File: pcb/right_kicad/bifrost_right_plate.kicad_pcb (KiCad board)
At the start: 2 copper layers, 148.8 x 87.6 mm, 23 parts

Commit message: Update PCB designs
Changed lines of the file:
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@@
 			(layer "F.SilkS"
 				(type "Top Silk Screen")
+				(color "White")
 			)
 			(layer "F.Paste"
@@
 			(layer "F.Mask"
 				(type "Top Solder Mask")
+				(color "Black")
 				(thickness 0.01)
 			)
@@
 			(layer "dielectric 1"
 				(type "core")
+				(color "Aluminum")
 				(thickness 1.11)
 				(material "FR4")
@@
 			(layer "B.Mask"
 				(type "Bottom Solder Mask")
+				(color "Black")
 				(thickness 0.01)
 			)
@@
 			(layer "B.SilkS"
 				(type "Bottom Silk Screen")
+				(color "White")
 			)
 			(copper_finish "None")
@@
 		(capping no)
 		(filling no)
+		(zone_defaults)
 		(pcbplotparams
 			(layerselection 0x00000000_00000000_55555555_5755f5ff)
@@
 		(end -134.542277 8.653086)
 		(stroke
-			(width 0)
+			(width 0.1)
 			(type default)
 		)
@@
 		(end -136.326562 11.380429)
 		(stroke
-			(width 0)
+			(width 0.1)
 			(type default)
 		)
@@
 		(end -136.326563 72.209898)
 		(stroke
-			(width 0)
+			(width 0.1)
 			(type default)
 		)
@@
 		(end -135.961405 73.638355)
 		(stroke
-			(width 0)
+			(width 0.1)
 			(type default)
 		)
@@
 		(end -33.3375 -12.501562)
 		(stroke
-			(width 0)
+			(width 0.1)
 			(type default)
 		)
@@
 		(end -135.56636 74.360548)
 		(stroke
-			(width 0)
+			(width 0.1)
 			(type default)
 		)
@@
 		(end -133.349999 70.238699)
 		(stroke
-			(width 0)
+			(width 0.1)
 			(type default)
 		)
@@
 		(end -133.681091 74.91259)
 		(stroke
-			(width 0)
+			(width 0.1)
 			(type default)
 		)
@@
 		(end -53.80468 48.117266)
 		(stroke
-			(width 0)
+			(width 0.1)
 			(type default)
 		)
@@
 		(end -116.679234 3.694859)
 		(stroke
-			(width 0)
+			(width 0.1)
 			(type default)
 		)
@@
 		(end -50.119883 50.915685)
 		(stroke
-			(width 0)
+			(width 0.1)
 			(type default)
 		)
@@
 		(end -50.119883 50.915685)
 		(stroke
-			(width 0)
+			(width 0.1)
 			(type default)
 		)
@@
 		(end -47.10797 68.939307)
 		(stroke
-			(width 0)
+			(width 0.1)
 			(type default)
 		)
@@
 		(end 9.525 -12.501563)
 		(stroke
-			(width 0)
+			(width 0.1)
 			(type default)
 		)
@@
 		(end -45.637701 70.0958)
 		(stroke
-			(width 0)
+			(width 0.1)
 			(type default)
 		)
@@
 		(end 12.501563 -9.525)
 		(stroke
-			(width 0)
+			(width 0.1)
 			(type default)
 		)
@@
 		(end 9.525 -10.625)
 		(stroke
-			(width 0)
+			(width 0.1)
 			(type default)
 		)
@@
 		(end 9.525 65.575)
 		(stroke
-			(width 0)
+			(width 0.1)
 			(type default)
 		)
@@
 		(end -33.3375 69.651563)
 		(stroke
-			(width 0)
+			(width 0.1)
 			(type default)
 		)
@@
 		(end 12.501562 66.675)
 		(stroke
-			(width 0)
+			(width 0.1)
 			(type default)
 		)
@@
 		(end 9.525 69.651563)
 		(stroke
-			(width 0)
+			(width 0.1)
 			(type default)
 		)

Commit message: Update PCB and case designs
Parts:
- added REF**: MountingHole_2.2mm_M2, MountingHole:MountingHole_2.2mm_M2, F.Cu at (212.7, 126.2)
- added REF**: MountingHole_2.2mm_M2, MountingHole:MountingHole_2.2mm_M2, F.Cu at (69.9, 130.9)
- added REF**: MountingHole_2.2mm_M2, MountingHole:MountingHole_2.2mm_M2, F.Cu at (86.5, 64.3)
- added REF**: MountingHole_2.2mm_M2, MountingHole:MountingHole_2.2mm_M2, F.Cu at (212.7, 50.0)
- PH16: value R1C1 -> 1U
- PH17: value R1C2 -> 1U
- PH18: value R1C3 -> 1U
- PH19: value R1C4 -> 1U
- PH2: value R1C5 -> 1U
- PH20: value R1C0 -> 1U
- PH26: value R2C0 -> 1U
- PH27: value R2C1 -> 1U
- PH28: value R2C2 -> 1U
- PH29: value R2C3 -> 1U
- PH3: value R3C5 -> 1U
- PH30: value R2C4 -> 1U
- PH36: value R3C0 -> 1U
- PH37: value R3C1 -> 1U
- PH38: value R3C2 -> 1U
- PH39: value R3C3 -> 1U
- PH4: value R3C6 -> 1U
- PH40: value R3C4 -> 1U
- PH46: value R4C4 -> 1U
- PH49: value R1C6 -> 1.5U
- PH5: value R4C5 -> 1U
- PH50: value R2C6 -> 2.25U
- PH6: value R4C6 -> 1U
- moved PH17 211.7 mm to (117.4, 65.3)
- moved PH18 211.7 mm to (136.3, 61.9)
- moved PH19 211.7 mm to (155.4, 60.0)
- moved PH20 211.7 mm to (80.7, 76.7)
- moved PH26 211.7 mm to (85.2, 95.4)
- moved PH28 211.7 mm to (122.0, 83.8)
- moved PH29 211.7 mm to (141.0, 80.5)
- moved PH3 211.7 mm to (184.2, 97.6)
- moved PH30 211.7 mm to (160.2, 78.8)
- moved PH36 211.7 mm to (89.8, 114.2)
- moved PH38 211.7 mm to (126.6, 102.3)
- moved PH39 211.7 mm to (145.7, 99.1)
- moved PH4 211.7 mm to (203.2, 97.6)
- moved PH40 211.7 mm to (165.0, 97.7)
- moved PH46 211.7 mm to (165.0, 116.7)
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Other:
- outline, holes or cut-outs redrawn

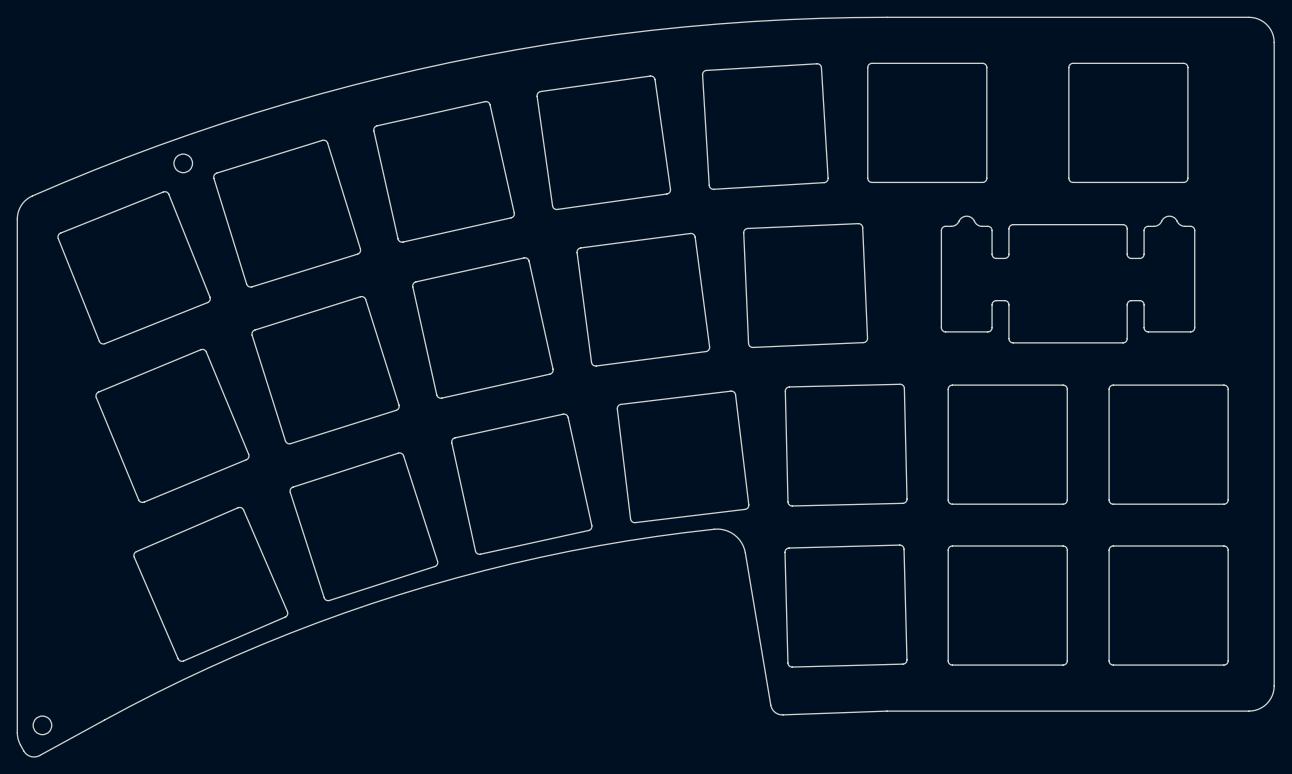
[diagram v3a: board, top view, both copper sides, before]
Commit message: Update case and plate designs
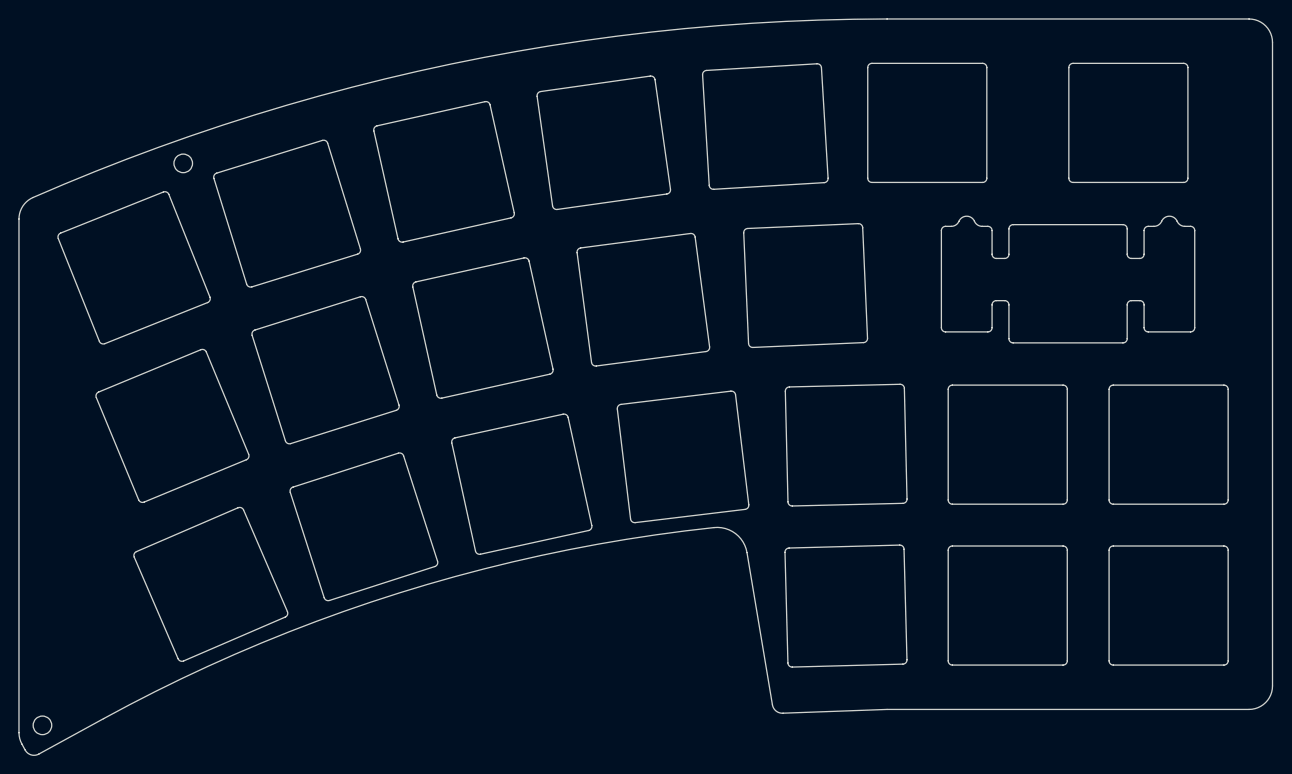
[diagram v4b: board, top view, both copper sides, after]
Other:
- board size 148.8 x 87.6 mm -> 148.4 x 87.2 mm
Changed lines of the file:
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@@
 		)
 		(fp_line
-			(start -6.55 -7.050002)
+			(start -6.55 -7.050003)
 			(end 6.55 -7.05)
 			(stroke
@@
 		)
 		(fp_line
-			(start 6.55 7.050002)
+			(start 6.55 7.050003)
 			(end -6.55 7.05)
 			(stroke
@@
 		)
 		(fp_line
-			(start 7.050002 -6.55)
+			(start 7.050003 -6.55)
 			(end 7.05 6.55)
 			(stroke
@@
 			(start -7.05 -6.55)
 			(mid -6.903553 -6.903553)
-			(end -6.55 -7.050002)
+			(end -6.55 -7.050003)
 			(stroke
 				(width 0.05)
@@
 		(fp_arc
 			(start -7.05 -6.55)
-			(mid -6.903555 -6.903553)
+			(mid -6.903556 -6.903553)
 			(end -6.55 -7.05)
 			(stroke
@@
 	)
 	(gr_arc
-		(start 66.873938 70.911679)
-		(mid 67.359636 69.282103)
-		(end 68.658223 68.184336)
+		(start 67.071875 70.911679)
+		(mid 67.525193 69.390741)
+		(end 68.737208 68.366158)
 		(stroke
 			(width 0.1)
@@
 	)
 	(gr_line
-		(start 66.873937 131.741148)
-		(end 66.873938 70.911679)
+		(start 67.071875 131.741148)
+		(end 67.071875 70.911679)
 		(stroke
 			(width 0.1)
@@
 	)
 	(gr_arc
-		(start 67.239095 133.169605)
-		(mid 66.966671 132.478344)
-		(end 66.873937 131.741148)
+		(start 67.412689 133.074375)
+		(mid 67.158427 132.429197)
+		(end 67.071875 131.741148)
 		(stroke
 			(width 0.1)
@@
 	)
 	(gr_line
-		(start 67.63414 133.891798)
-		(end 67.239095 133.169605)
+		(start 67.807733 133.796568)
+		(end 67.412689 133.074375)
 		(stroke
 			(width 0.1)
@@
 	)
 	(gr_arc
-		(start 68.658223 68.184336)
-		(mid 118.166951 52.37489)
-		(end 169.863 47.029688)
+		(start 68.737208 68.366158)
+		(mid 118.207053 52.569129)
+		(end 169.862501 47.228124)
 		(stroke
 			(width 0.1)
@@
 	)
 	(gr_arc
-		(start 69.519409 134.44384)
-		(mid 68.462443 134.558271)
-		(end 67.63414 133.891798)
+		(start 69.423678 134.269746)
+		(mid 68.517708 134.367829)
+		(end 67.807733 133.796568)
 		(stroke
 			(width 0.1)
@@
 	)
 	(gr_line
-		(start 77.17953 130.253699)
-		(end 69.519409 134.44384)
+		(start 77.083797 130.079604)
+		(end 69.423678 134.269746)
 		(stroke
 			(width 0.1)
@@
 	)
 	(gr_arc
-		(start 77.17953 130.253699)
-		(mid 112.169708 115.379561)
-		(end 149.39582 107.648516)
+		(start 77.083797 130.079604)
+		(mid 112.109927 115.190184)
+		(end 149.37429 107.451197)
 		(stroke
 			(width 0.1)
@@
 	)
 	(gr_arc
-		(start 149.39582 107.648516)
-		(mid 151.793591 108.316442)
-		(end 153.080617 110.446935)
+		(start 149.37429 107.451197)
+		(mid 151.913106 108.158412)
+		(end 153.27584 110.414226)
 		(stroke
 			(width 0.1)
@@
 	)
 	(gr_line
-		(start 156.09253 128.470557)
-		(end 153.080617 110.446935)
+		(start 156.287755 128.43785)
+		(end 153.27584 110.414226)
 		(stroke
 			(width 0.1)
@@
 	)
 	(gr_arc
-		(start 157.562799 129.62705)
-		(mid 156.603814 129.333389)
-		(end 156.09253 128.470557)
+		(start 157.547984 129.42913)
+		(mid 156.725997 129.17742)
+		(end 156.287755 128.43785)
 		(stroke
 			(width 0.1)
@@
 	)
 	(gr_line
-		(start 169.863 47.029688)
-		(end 212.7255 47.029687)
+		(start 169.862501 47.228124)
+		(end 212.725 47.228125)
 		(stroke
 			(width 0.1)
@@
 	)
 	(gr_line
-		(start 169.863 129.182813)
-		(end 157.562799 129.62705)
+		(start 169.8625 128.984376)
+		(end 157.547984 129.42913)
 		(stroke
 			(width 0.1)
@@
 	)
 	(gr_arc
-		(start 212.7255 47.029687)
-		(mid 214.830224 47.901526)
-		(end 215.702063 50.00625)
+		(start 212.725 47.228125)
+		(mid 214.6894 48.041836)
+		(end 215.503125 50.00625)
 		(stroke
 			(width 0.1)
@@
 	)
 	(gr_line
-		(start 212.7255 129.182813)
-		(end 169.863 129.182813)
+		(start 212.725 128.984376)
+		(end 169.8625 128.984376)
 		(stroke
 			(width 0.1)
@@
 	)
 	(gr_line
-		(start 215.702063 50.00625)
-		(end 215.702062 126.20625)
+		(start 215.503125 50.00625)
+		(end 215.503126 126.20625)
 		(stroke
 			(width 0.1)
@@
 	)
 	(gr_arc
-		(start 215.702062 126.20625)
-		(mid 214.830247 128.310997)
-		(end 212.7255 129.182813)
+		(start 215.503126 126.20625)
+		(mid 214.689432 128.170681)
+		(end 212.725 128.984376)
 		(stroke
 			(width 0.1)
@@
 	)
 	(group ""
-		(members "05205f61-b1f3-4ac0-8d08-905ff259f779" "0eb6174c-08d9-49a6-b43b-26562caf9cb0"
-			"0fccac3d-4f03-4dae-b8bb-0b55bf84f5bb" "25277f79-f406-4547-bf54-c42eee6305e4"
-			"5bfde130-cea9-4220-ba5f-ae05cf9bd949" "6006cb95-fb72-4ff4-ad12-af0703871a8c"
-			"7580f186-9d17-4c58-85b1-be262a8b06a4" "8cd59c88-d864-4b33-b62d-2d688135f6a3"
-			"907f68c1-14c5-44cc-b531-f83f5e247b25" "a2a41146-9c32-42cc-989f-50a6818a1920"
-			"a6b365ec-06ac-4b27-8f29-405e2a253ecc" "aed5970d-0e8f-4829-abd1-e9478ae47059"
-			"cace9732-bd5e-42ed-9ef5-665e176be887" "d1e3c43a-c882-4823-944e-67de9eced70b"
-			"d30d92f5-68d0-4685-a739-ec7837e45be0" "e2d82f6e-af53-4930-9027-cfa645b7df42"
-			"fbdac2ce-d1dc-4cf6-90ae-2241300d7ddc"
+		(members "068551cd-b98d-4d11-bc05-51a5e18aaf50" "0c1d201c-a72c-44ae-9a11-bc7056553b03"
+			"0ec73f2a-5642-4d2b-b2e6-3339372fdbfb" "29500b76-82ae-400b-afe1-cbf4491517f8"
+			"462d9c15-4ea2-4144-b638-1068ea8c0ccd" "477ccc58-686d-4d3e-8bce-5e1c15352b5e"
+			"594a3cd7-e76b-4329-9f79-3c448590a85e" "60bfa5f7-607d-4bd0-b87e-24dc4babe0fe"
+			"74ca832a-3957-4c4d-8bfe-6299b8b6a768" "9204d815-02dc-4e0f-981e-b6026e78c3e7"
+			"93ef8db7-efe5-43cf-968f-b134248e0dc3" "945683d4-b1df-40b2-87ab-89757708c649"
+			"99e70592-c986-4c7b-a29d-e71080e82b58" "aa0f14ed-5eaa-4edc-ad59-8561614b38f3"
+			"e01bc9c0-2894-4b89-b29a-3185ffda7c25" "e672b342-ce5d-4ac0-94c5-bc2c394b090d"
+			"e92e23e9-0dfd-4cae-a427-998ad65c2936"
 		)
 	)
